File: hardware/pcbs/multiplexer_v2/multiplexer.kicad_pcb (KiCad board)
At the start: 2 copper layers, 81.3 x 88.9 mm, 22 parts, among them K1 CONN_3, M1 VAL**, M2 VAL**, M3 VAL**, P1 CONN_5X2, P2 CONN_5X2, P3 CONN_2, P4 CONN_2, P5 CONN_5X2, U1 ADG44X, U2 ADG44X, U3 ADG44X, U4 ADG44X

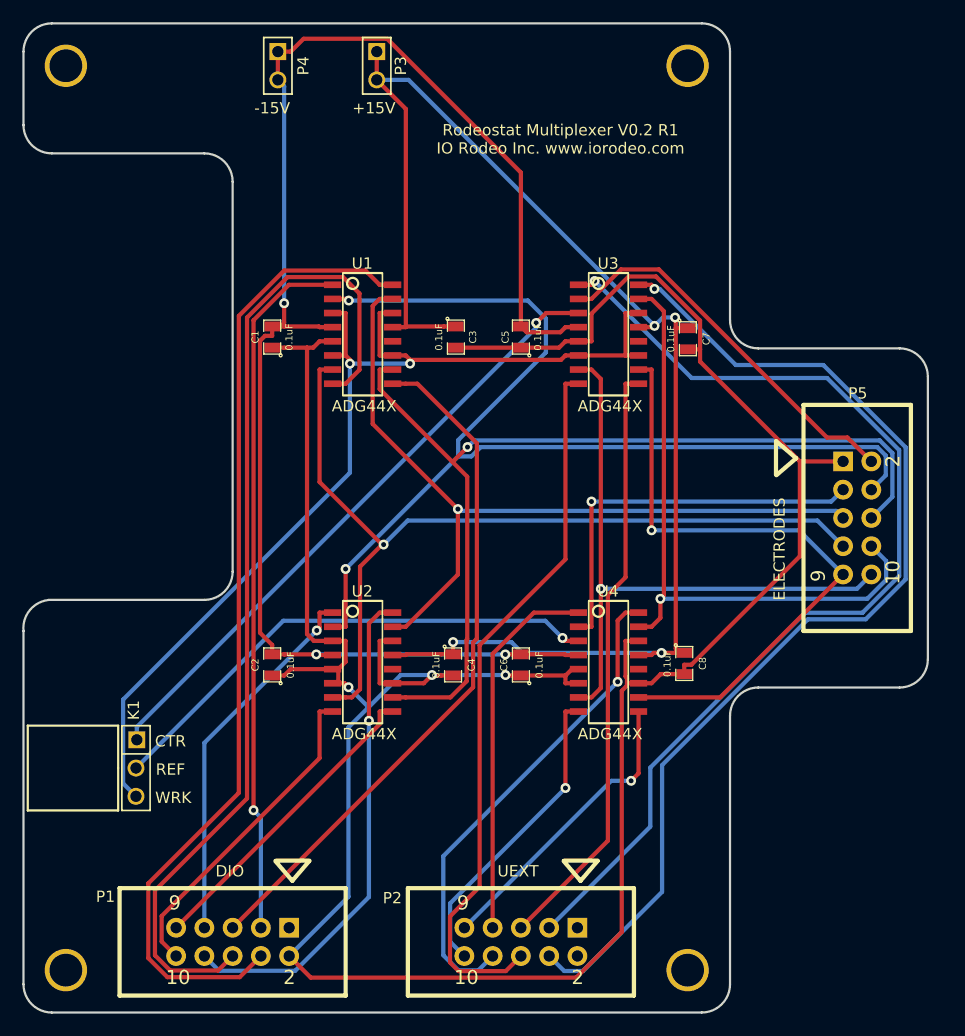
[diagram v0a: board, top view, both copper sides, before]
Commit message: Modified v0.2 of multiplexer. Extended tab with 5x2 header connector to deal with interference issue. Finished the two initial multiplexer adapter pcbs - mux_to_term and mux_to_3pin.
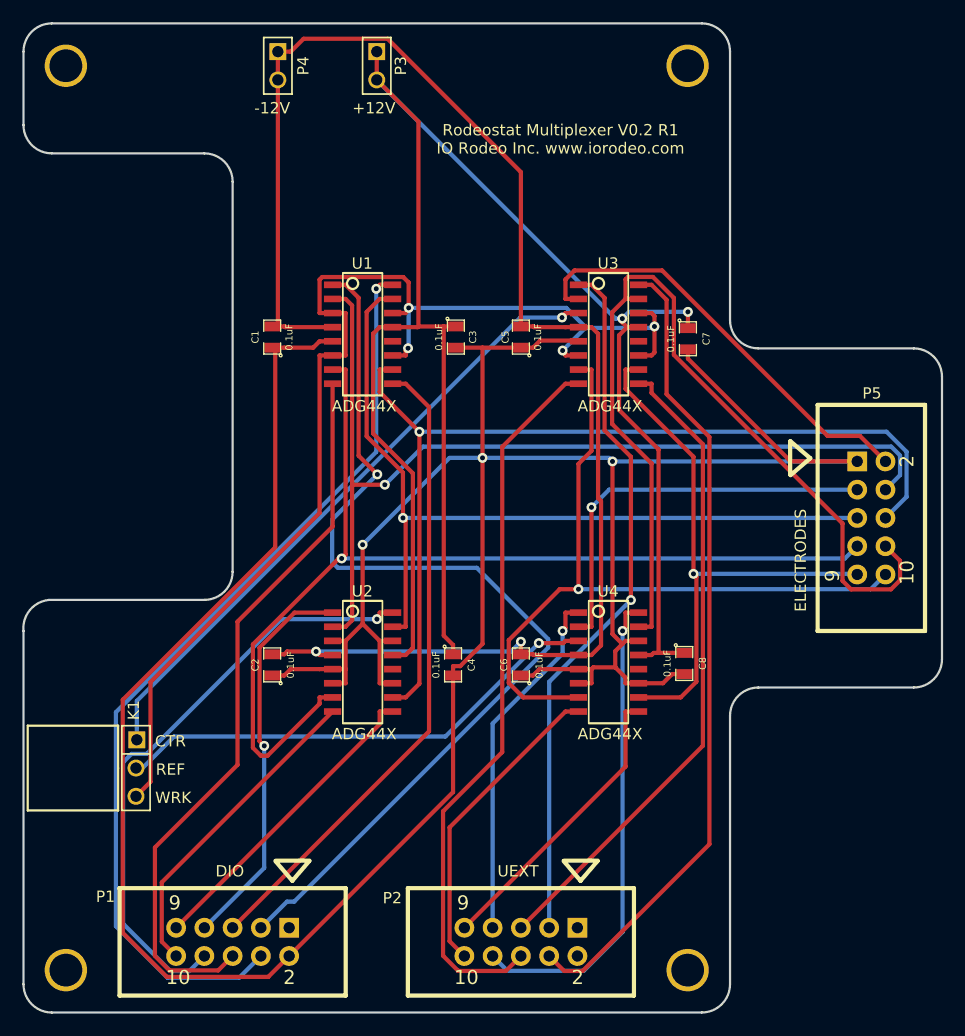
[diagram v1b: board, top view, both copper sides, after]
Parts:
- moved P5 1.27 mm to (152.4, 120.7)
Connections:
- net /+15V renamed /+12V
- net /-15V renamed /-12V
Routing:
- net /GND: track 247.2 -> 292.5 mm
- net /+12V: track 130.6 -> 171.3 mm, vias 4 -> 2
- net /D3: track 94.3 -> 63.5 mm
- net /D24: track 63.3 -> 88.3 mm
- net /D27: track 90.8 -> 66.1 mm
- net /WRK_5: track 57.3 -> 81.9 mm, vias 1 -> 0
- net /D4: track 95.8 -> 73.3 mm, vias 1 -> 0
- net /WRK_4: track 79.1 -> 95.5 mm
- net /WRK: track 94.2 -> 109.7 mm, vias 2 -> 4
- net /WRK_1: track 98.9 -> 86.9 mm, vias 2 -> 1
- net /WRK_7: track 57.3 -> 68.3 mm
- net /D29: track 45.2 -> 54.1 mm
- net /WRK_6: track 57.4 -> 52.4 mm
- net /D19: track 54.0 -> 58.8 mm
- net /CTR_SW: track 34.6 -> 39.1 mm
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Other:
- board size 81.3 x 88.9 mm -> 82.6 x 88.9 mm
- board text added: "+12V"
- board text added: "-12V"
- board text removed: "+15V"
- board text removed: "-15V"
